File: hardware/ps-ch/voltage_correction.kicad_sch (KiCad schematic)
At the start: 46 parts, among them Q10 MMBT3904, Q5 MMBT3906, Q6 MMBT3906, Q7 MMBT3904, Q8 MMBT3904, U7 OPA992IDCKR, U8 OPA992IDCKR, U9 OPA992IDCKR

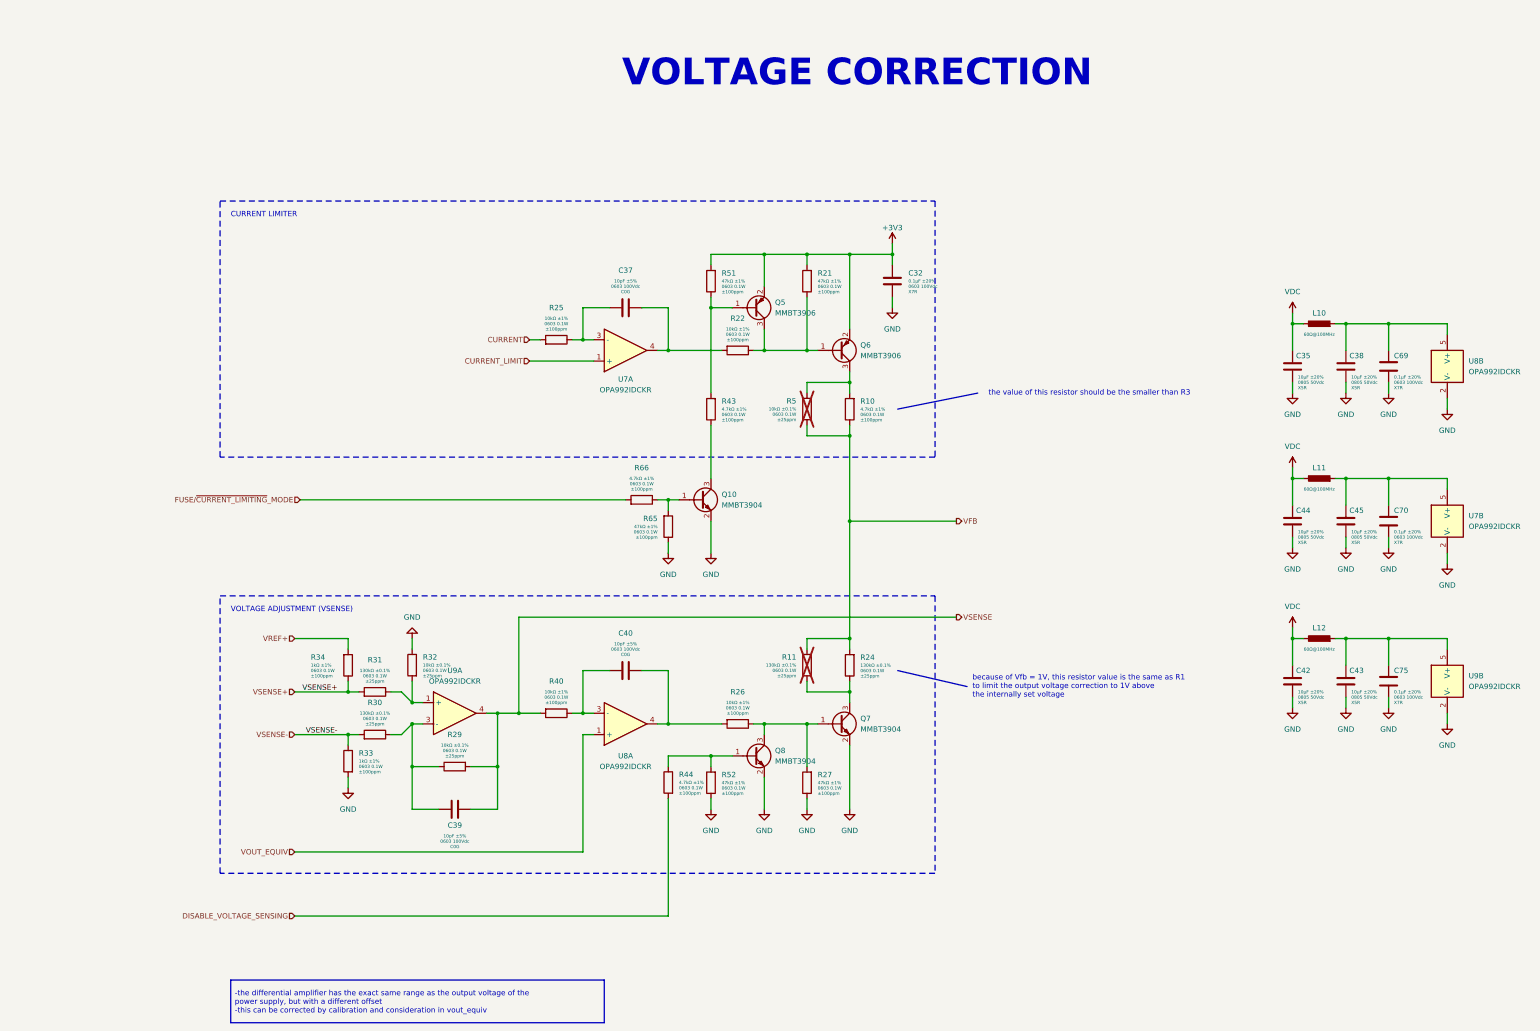
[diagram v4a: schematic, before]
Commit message: changed voltage regulation (preregulator)
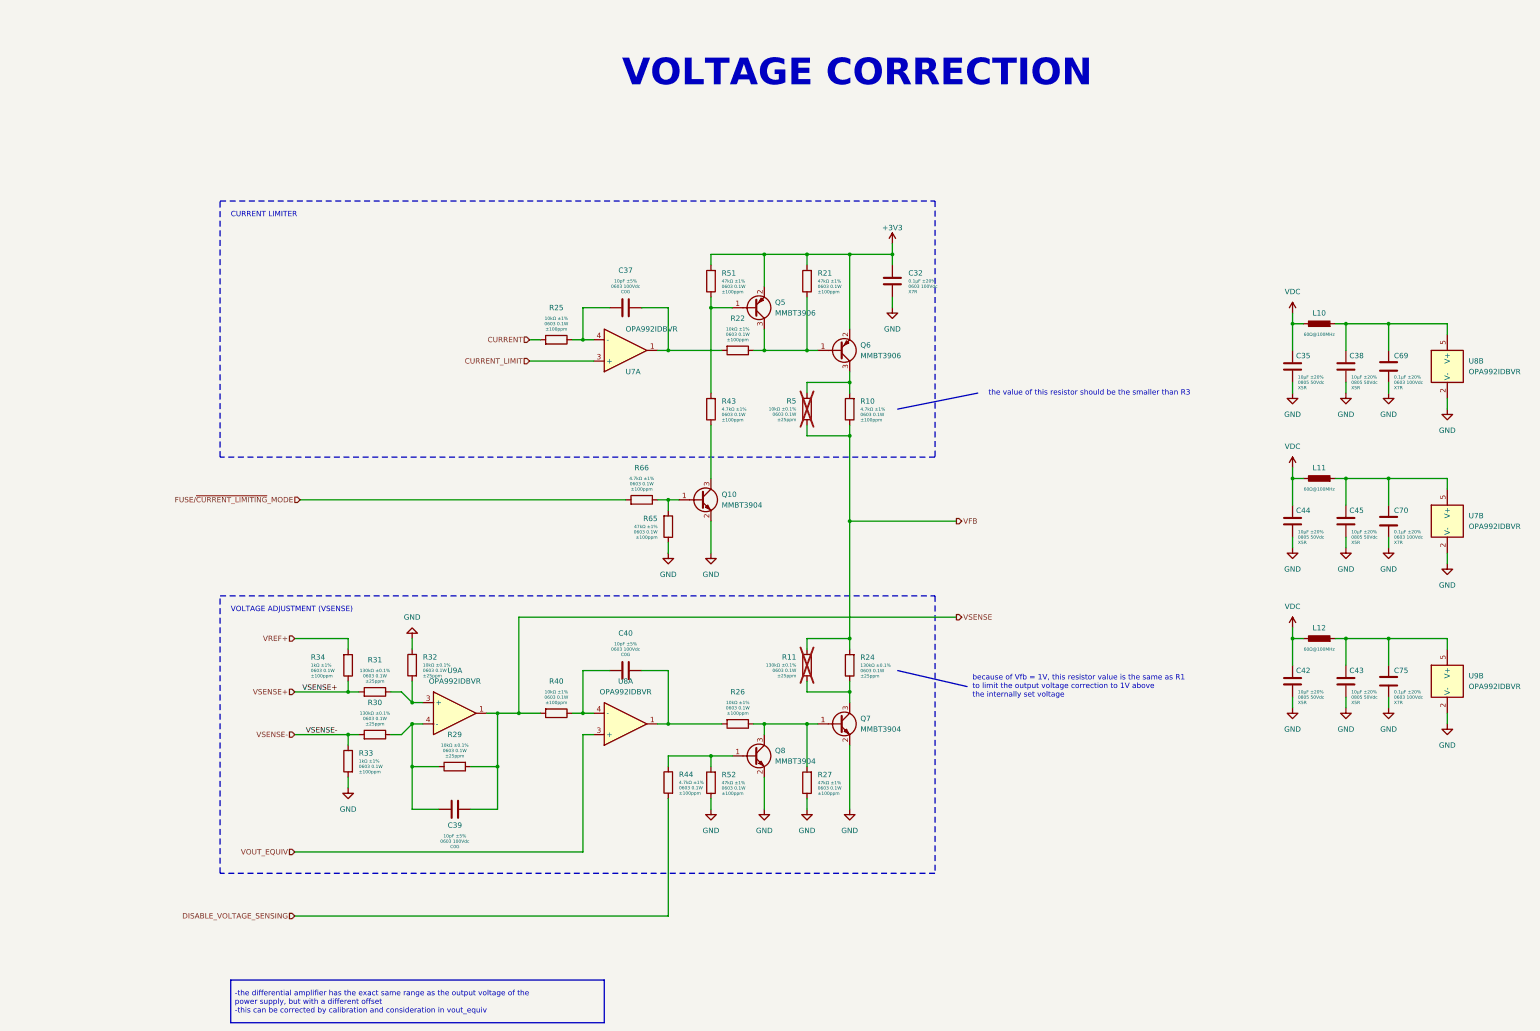
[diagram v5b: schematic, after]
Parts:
- U7, U8, U9: value OPA992IDCKR -> OPA992IDBVR; footprint (none) -> Package_TO_SOT_SMD:SOT-23-5; symbol ps-ch:OPA992IDCKR -> ps-ch:OPA992IDBVR; Manufacturer (none) -> Texas Instruments; Manufacturer Part Number (none) -> OPA992IDBVR
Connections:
- net CURRENT_LIMIT: now also U7.3 (+); no longer U7.1 (+)
- net VOUT_EQUIV: now also U8.3 (+); no longer U8.1 (+)
- net VSENSE: now also U9.1; no longer U9.4
- net at R31.1, R32.2: now also U9.3 (+); no longer U9.1 (+)
- net at C39.2, R29.1, R30.1: now also U9.4 (-); no longer U9.3 (-)
- net at C40.1, R40.1: now also U8.4 (-); no longer U8.3 (-)
- net at C40.2, R26.2: now also U8.1; no longer U8.4
- net at C37.1, R22.2: now also U7.1; no longer U7.4
- net at C37.2, R25.1: now also U7.4 (-); no longer U7.3 (-)
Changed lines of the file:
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@@
 	)
 	(symbol
-		(lib_id "ps-ch:OPA992IDCKR")
+		(lib_id "ps-ch:OPA992IDBVR")
 		(at 116.84 190.5 0)
 		(unit 1)
@@
 			)
 		)
-		(property "Value" "OPA992IDCKR"
+		(property "Value" "OPA992IDBVR"
 			(at 116.84 182.88 0)
 			(effects
@@
 			)
 		)
-		(property "Footprint" ""
-			(at 116.84 190.5 0)
+		(property "Footprint" "Package_TO_SOT_SMD:SOT-23-5"
+			(at 116.84 180.34 0)
 			(effects
 				(font
@@
 			)
 		)
-		(property "Datasheet" "~"
-			(at 116.84 190.5 0)
+		(property "Datasheet" "https://www.ti.com/lit/ds/symlink/opa2992.pdf?ts=1758720881687&ref_url=https%253A%252F%252Fco.mouser.com%252F"
+			(at 116.84 177.8 0)
 			(effects
 				(font
@@
 			)
 		)
+		(property "Manufacturer" "Texas Instruments"
+			(at 116.84 172.72 0)
+			(effects
+				(font
+					(size 1.27 1.27)
+				)
+				(hide yes)
+			)
+		)
+		(property "Manufacturer Part Number" "OPA992IDBVR"
+			(at 116.84 175.26 0)
+			(effects
+				(font
+					(size 1.27 1.27)
+				)
+				(hide yes)
+			)
+		)
 		(pin "5"
 		)
@@
 	)
 	(symbol
-		(lib_id "ps-ch:OPA992IDCKR")
+		(lib_id "ps-ch:OPA992IDBVR")
 		(at 157.48 193.04 0)
 		(mirror x)
@@
 		(fields_autoplaced yes)
 		(property "Reference" "U8"
-			(at 157.48 200.66 0)
+			(at 157.48 182.88 0)
 			(effects
 				(font
@@
 			)
 		)
-		(property "Value" "OPA992IDCKR"
-			(at 157.48 203.2 0)
+		(property "Value" "OPA992IDBVR"
+			(at 157.48 185.42 0)
 			(effects
 				(font
@@
 			)
 		)
-		(property "Footprint" ""
-			(at 157.48 193.04 0)
+		(property "Footprint" "Package_TO_SOT_SMD:SOT-23-5"
+			(at 157.48 203.2 0)
 			(effects
 				(font
@@
 			)
 		)
-		(property "Datasheet" "~"
-			(at 157.48 193.04 0)
+		(property "Datasheet" "https://www.ti.com/lit/ds/symlink/opa2992.pdf?ts=1758720881687&ref_url=https%253A%252F%252Fco.mouser.com%252F"
+			(at 157.48 205.74 0)
 			(effects
 				(font
@@
 			)
 		)
+		(property "Manufacturer" "Texas Instruments"
+			(at 157.48 210.82 0)
+			(effects
+				(font
+					(size 1.27 1.27)
+				)
+				(hide yes)
+			)
+		)
+		(property "Manufacturer Part Number" "OPA992IDBVR"
+			(at 157.48 208.28 0)
+			(effects
+				(font
+					(size 1.27 1.27)
+				)
+				(hide yes)
+			)
+		)
 		(pin "3"
 		)
@@
 	)
 	(symbol
-		(lib_id "ps-ch:OPA992IDCKR")
+		(lib_id "ps-ch:OPA992IDBVR")
 		(at 353.06 182.88 0)
 		(unit 2)
@@
 			)
 		)
-		(property "Value" "OPA992IDCKR"
+		(property "Value" "OPA992IDBVR"
 			(at 358.14 184.1499 0)
 			(effects
@@
 			)
 		)
-		(property "Footprint" ""
-			(at 353.06 182.88 0)
+		(property "Footprint" "Package_TO_SOT_SMD:SOT-23-5"
+			(at 353.06 172.72 0)
 			(effects
 				(font
@@
 			)
 		)
-		(property "Datasheet" "~"
-			(at 353.06 182.88 0)
+		(property "Datasheet" "https://www.ti.com/lit/ds/symlink/opa2992.pdf?ts=1758720881687&ref_url=https%253A%252F%252Fco.mouser.com%252F"
+			(at 353.06 170.18 0)
 			(effects
 				(font
@@
 			)
 		)
+		(property "Manufacturer" "Texas Instruments"
+			(at 353.06 165.1 0)
+			(effects
+				(font
+					(size 1.27 1.27)
+				)
+				(hide yes)
+			)
+		)
+		(property "Manufacturer Part Number" "OPA992IDBVR"
+			(at 353.06 167.64 0)
+			(effects
+				(font
+					(size 1.27 1.27)
+				)
+				(hide yes)
+			)
+		)
 		(pin "3"
 		)
@@
 	)
 	(symbol
-		(lib_id "ps-ch:OPA992IDCKR")
+		(lib_id "ps-ch:OPA992IDBVR")
 		(at 157.48 104.14 0)
 		(mirror x)
@@
 		(dnp no)
 		(property "Reference" "U7"
-			(at 157.48 110.998 0)
+			(at 157.48 109.22 0)
 			(effects
 				(font
 					(size 1.27 1.27)
 				)
+				(justify left)
 			)
 		)
-		(property "Value" "OPA992IDCKR"
-			(at 157.48 113.538 0)
+		(property "Value" "OPA992IDBVR"
+			(at 157.48 99.06 0)
 			(effects
 				(font
 					(size 1.27 1.27)
 				)
+				(justify left)
 			)
 		)
-		(property "Footprint" ""
-			(at 157.48 104.14 0)
+		(property "Footprint" "Package_TO_SOT_SMD:SOT-23-5"
+			(at 157.48 114.3 0)
 			(effects
 				(font
@@
 			)
 		)
-		(property "Datasheet" "~"
-			(at 157.48 104.14 0)
+		(property "Datasheet" "https://www.ti.com/lit/ds/symlink/opa2992.pdf?ts=1758720881687&ref_url=https%253A%252F%252Fco.mouser.com%252F"
+			(at 157.48 116.84 0)
 			(effects
 				(font
@@
 			)
 		)
+		(property "Manufacturer" "Texas Instruments"
+			(at 157.48 121.92 0)
+			(effects
+				(font
+					(size 1.27 1.27)
+				)
+				(hide yes)
+			)
+		)
+		(property "Manufacturer Part Number" "OPA992IDBVR"
+			(at 157.48 119.38 0)
+			(effects
+				(font
+					(size 1.27 1.27)
+				)
+				(hide yes)
+			)
+		)
 		(pin "5"
 		)
@@
 	)
 	(symbol
-		(lib_id "ps-ch:OPA992IDCKR")
+		(lib_id "ps-ch:OPA992IDBVR")
 		(at 353.06 144.78 0)
 		(unit 2)
@@
 			)
 		)
-		(property "Value" "OPA992IDCKR"
+		(property "Value" "OPA992IDBVR"
 			(at 358.14 146.0499 0)
 			(effects
@@
 			)
 		)
-		(property "Footprint" ""
-			(at 353.06 144.78 0)
+		(property "Footprint" "Package_TO_SOT_SMD:SOT-23-5"
+			(at 353.06 134.62 0)
 			(effects
 				(font
@@
 			)
 		)
-		(property "Datasheet" "~"
-			(at 353.06 144.78 0)
+		(property "Datasheet" "https://www.ti.com/lit/ds/symlink/opa2992.pdf?ts=1758720881687&ref_url=https%253A%252F%252Fco.mouser.com%252F"
+			(at 353.06 132.08 0)
 			(effects
 				(font
@@
 			)
 		)
+		(property "Manufacturer" "Texas Instruments"
+			(at 353.06 127 0)
+			(effects
+				(font
+					(size 1.27 1.27)
+				)
+				(hide yes)
+			)
+		)
+		(property "Manufacturer Part Number" "OPA992IDBVR"
+			(at 353.06 129.54 0)
+			(effects
+				(font
+					(size 1.27 1.27)
+				)
+				(hide yes)
+			)
+		)
 		(pin "3"
 		)
@@
 	)
 	(symbol
-		(lib_id "ps-ch:OPA992IDCKR")
+		(lib_id "ps-ch:OPA992IDBVR")
 		(at 353.06 107.95 0)
 		(unit 2)
@@
 			)
 		)
-		(property "Value" "OPA992IDCKR"
+		(property "Value" "OPA992IDBVR"
 			(at 358.14 109.2199 0)
 			(effects
@@
 			)
 		)
-		(property "Footprint" ""
-			(at 353.06 107.95 0)
+		(property "Footprint" "Package_TO_SOT_SMD:SOT-23-5"
+			(at 353.06 97.79 0)
 			(effects
 				(font
@@
 			)
 		)
-		(property "Datasheet" "~"
-			(at 353.06 107.95 0)
+		(property "Datasheet" "https://www.ti.com/lit/ds/symlink/opa2992.pdf?ts=1758720881687&ref_url=https%253A%252F%252Fco.mouser.com%252F"
+			(at 353.06 95.25 0)
 			(effects
 				(font
@@
 			(effects
 				(font
+					(size 1.27 1.27)
+				)
+				(hide yes)
+			)
+		)
+		(property "Manufacturer" "Texas Instruments"
+			(at 353.06 90.17 0)
+			(effects
+				(font
+					(size 1.27 1.27)
+				)
+				(hide yes)
+			)
+		)
+		(property "Manufacturer Part Number" "OPA992IDBVR"
+			(at 353.06 92.71 0)
+			(effects
+				(font

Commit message: changed voltage sensing circuit
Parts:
- removed Q8: MMBT3904, Package_TO_SOT_SMD:SOT-23, symbol Transistor_BJT:MMBT3904
- removed R44: 4.7kΩ 0603 0.1W ±1% ±100ppm/°C, Resistor_SMD:R_0603_1608Metric, symbol ps-ch:4.7kΩ 0603 0.1W ±1% ±100ppm/°C
- removed R52: 47kΩ 0603 0.1W ±1% ±100ppm/°C, Resistor_SMD:R_0603_1608Metric, symbol ps-ch:47kΩ 0603 0.1W ±1% ±100ppm/°C
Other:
- moved on the sheet: C39, R29, R30, R31, R32, R33, R34, U9A

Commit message: first pcb sync
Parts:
- renumbered C32 to C76, C37 to C77, C35 to C78, C38 to C79, C69 to C80, C44 to C81, C45 to C82, C70 to C83, C40 to C84, C42 to C85, C43 to C86, C75 to C87, C39 to C88, L10 to L13, L11 to L14, L12 to L15, Q6 to Q10, Q10 to Q11, Q7 to Q12, Q5 to Q9, R51 to R61, R21 to R62, R25 to R63, R22 to R64, R43 to R65, R5 to R66, R10 to R67, R66 to R68, R65 to R69, R34 to R70, R32 to R71, R11 to R72, R24 to R73, R31 to R74, R40 to R75, R26 to R76, R30 to R77, R33 to R78, R29 to R79, R27 to R80, U7 to U15, U8 to U15, U9 to U16, U7 to U16, U8 to U17, U9 to U17
